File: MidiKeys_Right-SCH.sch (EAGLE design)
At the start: 7 parts

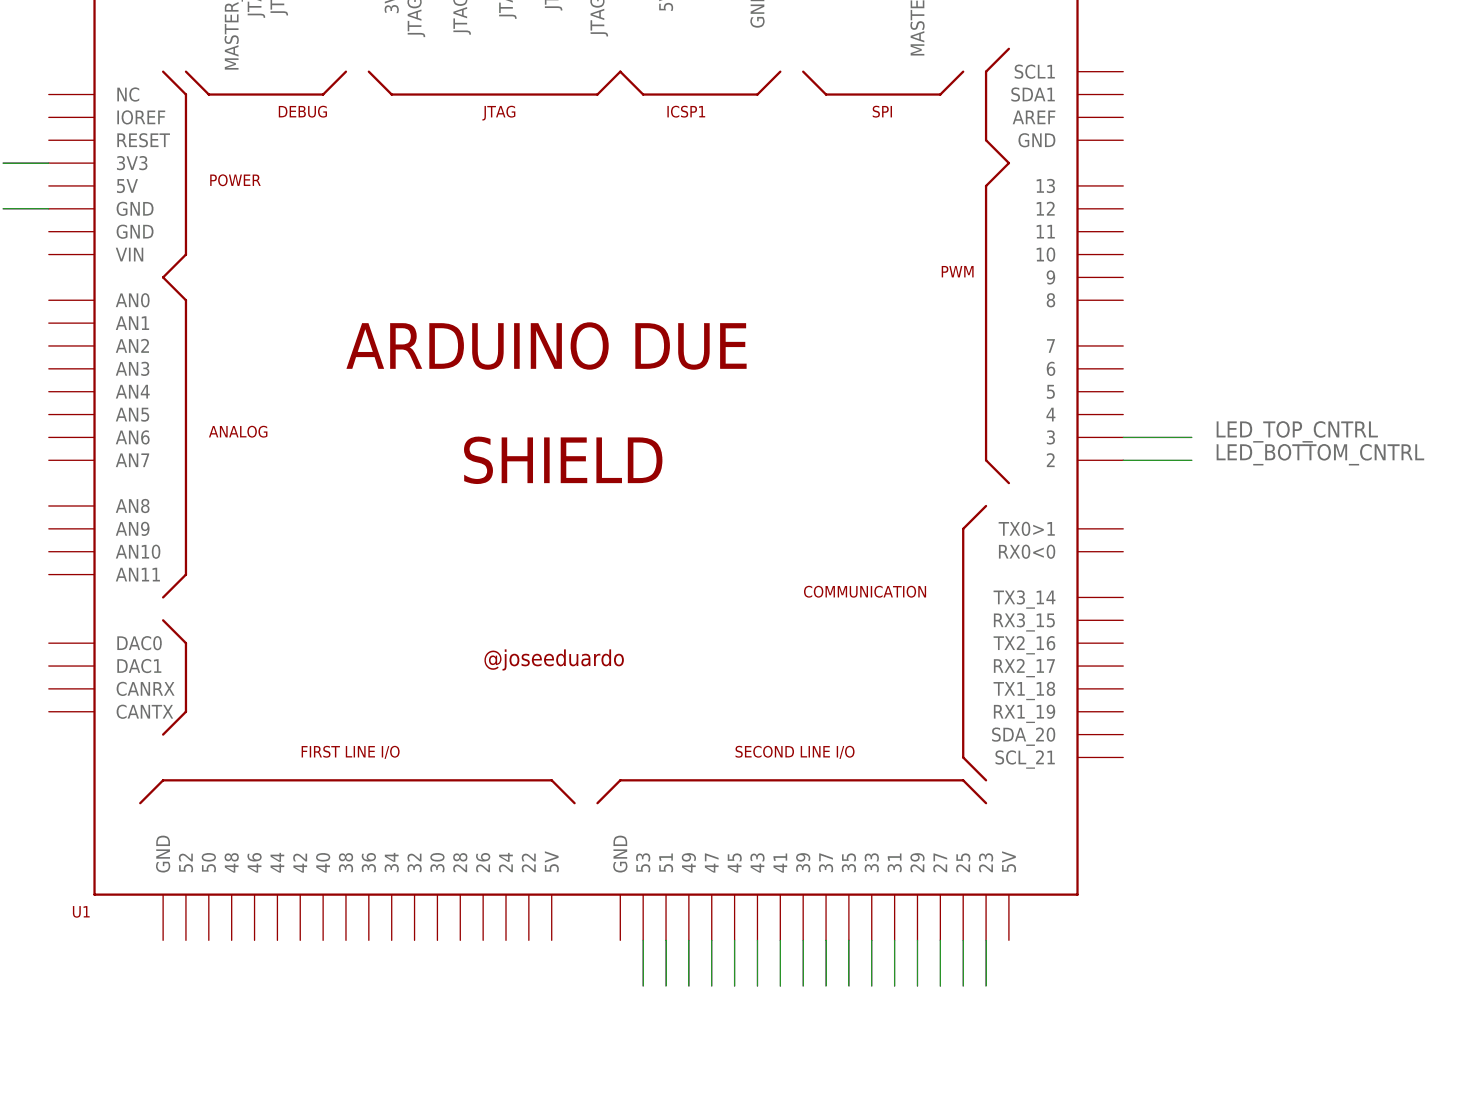
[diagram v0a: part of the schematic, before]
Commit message: added all key nets
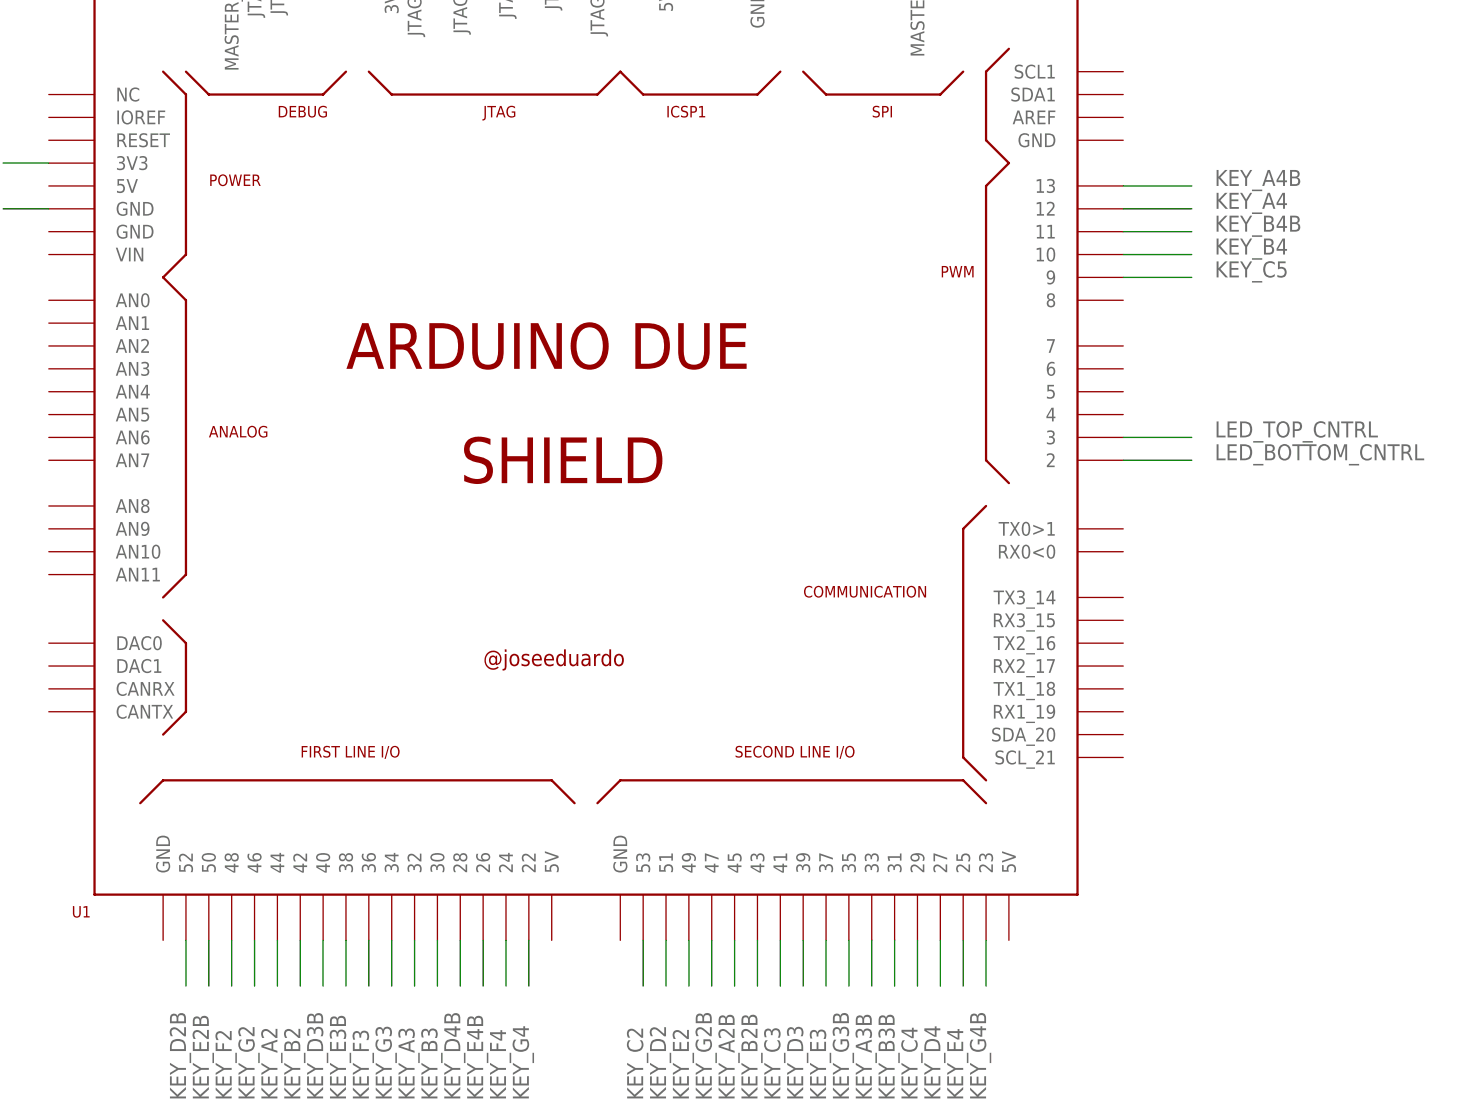
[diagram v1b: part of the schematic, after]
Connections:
- net N$10 renamed KEY_D3
- net N$11 renamed KEY_E3
- net N$12 renamed KEY_G3B
- net N$13 renamed KEY_A3B
- net N$14 renamed KEY_B3B
- net N$15 renamed KEY_C4
- net N$16 renamed KEY_D4
- net N$17 renamed KEY_E4
- net N$18 renamed KEY_G4B
- net N$2 renamed KEY_D2
- net N$3 renamed KEY_E2
- net N$6 renamed KEY_G2B
- net N$7 renamed KEY_A2B
- net N$8 renamed KEY_B2B
- net N$9 renamed KEY_C3
- removed net N$1: ARDUINO_DUE1.53
- new net KEY_A2: ARDUINO_DUE1.44
- new net KEY_A3: ARDUINO_DUE1.32
- new net KEY_A4: ARDUINO_DUE1.12
- new net KEY_A4B: ARDUINO_DUE1.13
- new net KEY_B2: ARDUINO_DUE1.42
- new net KEY_B3: ARDUINO_DUE1.30
- new net KEY_B4: ARDUINO_DUE1.10
- new net KEY_B4B: ARDUINO_DUE1.11
- new net KEY_C5: ARDUINO_DUE1.9
- new net KEY_D3B: ARDUINO_DUE1.40
- new net KEY_D4B: ARDUINO_DUE1.28
- new net KEY_E2B: ARDUINO_DUE1.50
- new net KEY_E3B: ARDUINO_DUE1.38
- new net KEY_E4B: ARDUINO_DUE1.26
- new net KEY_F2: ARDUINO_DUE1.48
- new net KEY_F3: ARDUINO_DUE1.36
- new net KEY_F4: ARDUINO_DUE1.24
- new net KEY_G2: ARDUINO_DUE1.46
- new net KEY_G3: ARDUINO_DUE1.34
- new net KEY_G4: ARDUINO_DUE1.22
- net KEY_C2: now also ARDUINO_DUE1.53
- net KEY_D2B: now also ARDUINO_DUE1.52

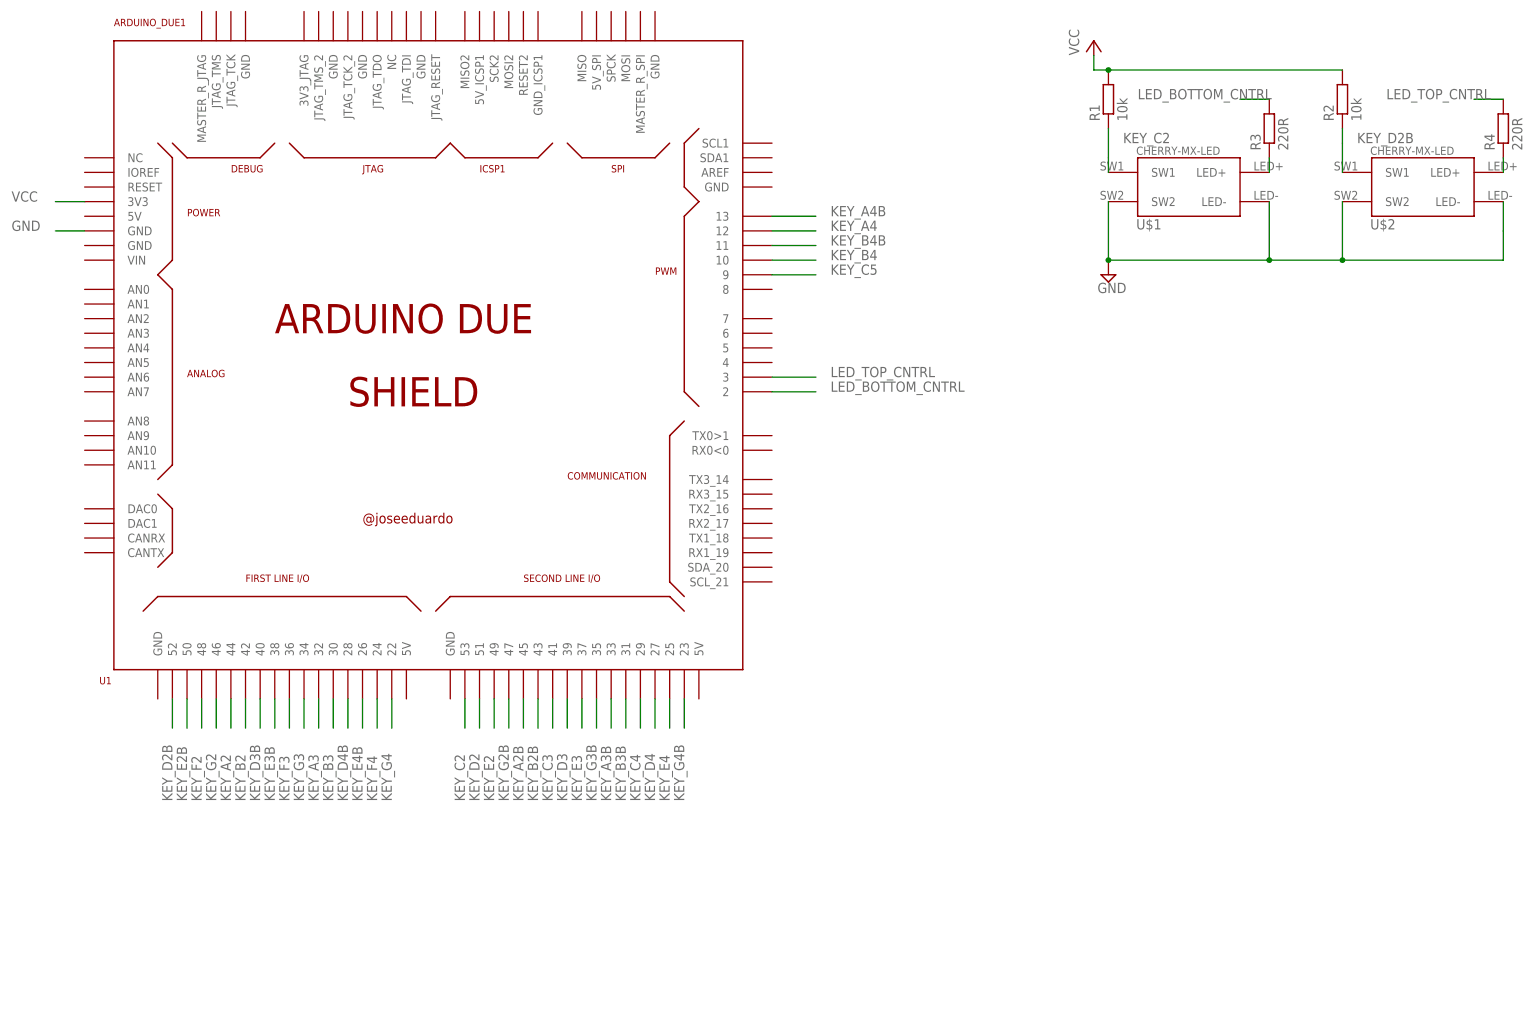
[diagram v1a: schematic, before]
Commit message: cleaned up keys - now adding all of them to schematic
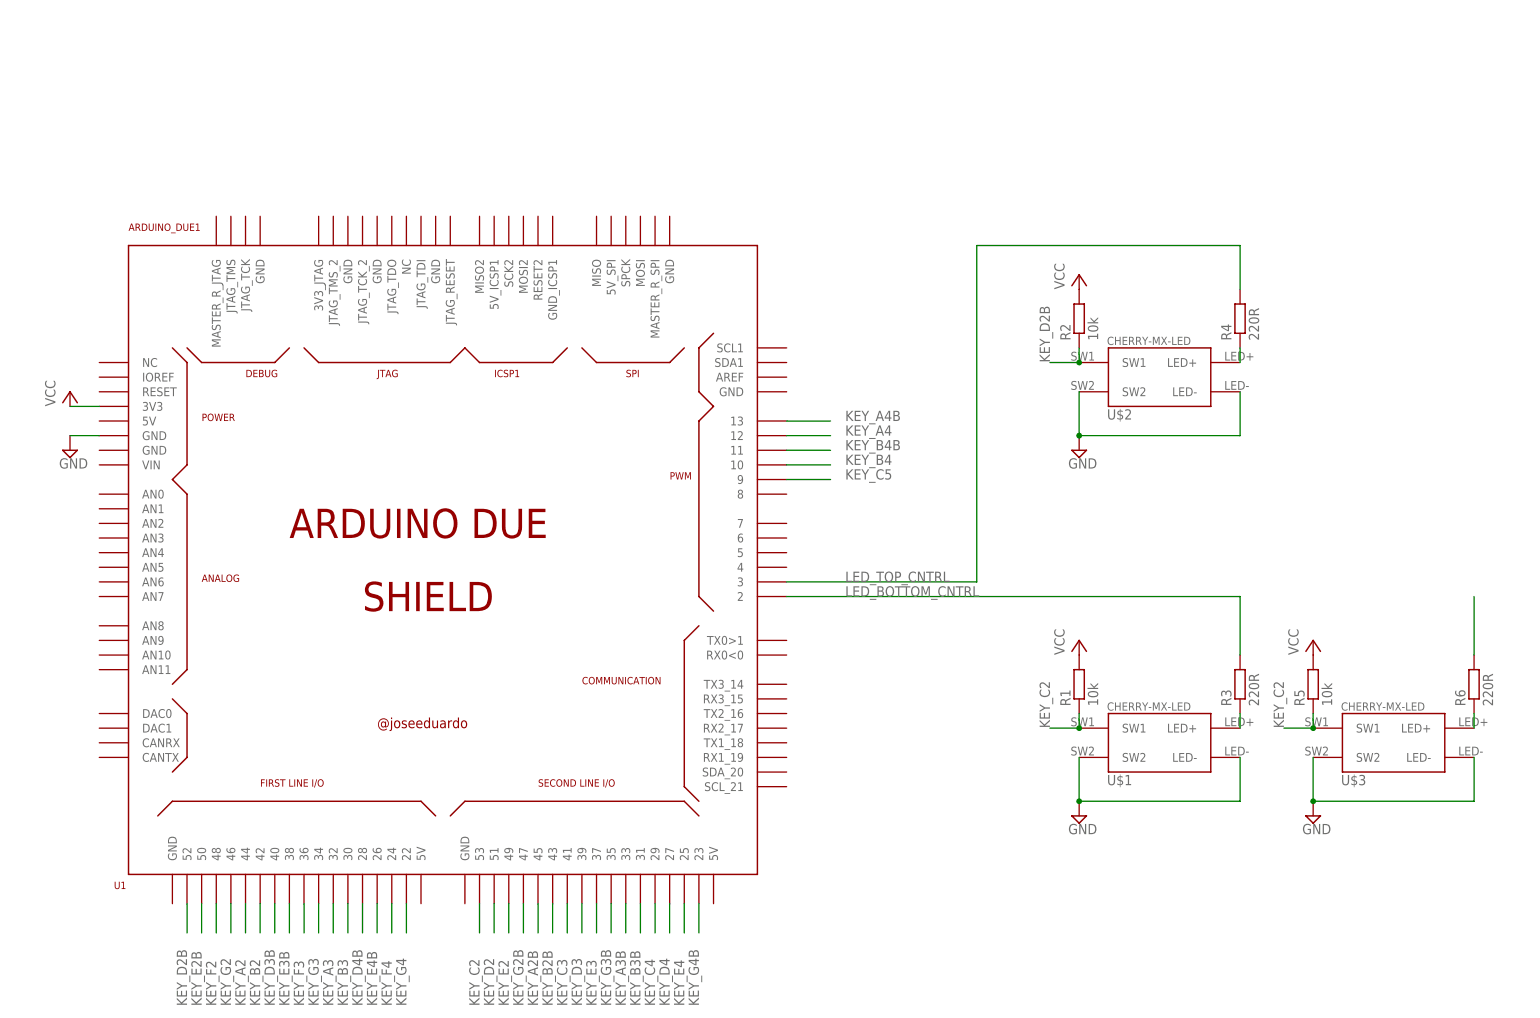
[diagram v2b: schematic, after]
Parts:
- added R5: 10k, resistor:R-EU_R0603
- added R6: 220R, resistor:R-EU_R0603
- added U$3: CHERRY-MX-LED, cherrymx:CHERRY-MX-LED
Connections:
- new net LED_BOTTOM_CNTRL1: R6.2
- new net N$1: R6.1, U$3.LED+
- net GND: now also U$3.LED-, U$3.SW2
- net KEY_C2: now also R5.1, U$3.SW1
- net VCC: now also R5.2
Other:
- moved on the sheet: ARDUINO_DUE1, R1, R2, R3, R4, U$1, U$2

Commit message: created bottom row of keys in schematic
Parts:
- added R10, R12, R14, R16, R18, R20, R22, R24, R26, R28, R30, R32, R34, R36, R38, R40, R42, R44, R46, R48, R8: 220R, resistor:R-EU_R0603
- added R11, R13, R15, R17, R19, R21, R23, R25, R27, R29, R31, R33, R35, R37, R39, R41, R43, R45, R47, R7, R9: 10k, resistor:R-EU_R0603
- added U$10, U$11, U$12, U$13, U$14, U$15, U$16, U$17, U$18, U$19, U$20, U$21, U$22, U$23, U$24, U$4, U$5, U$6, U$7, U$8, U$9: CHERRY-MX-LED, cherrymx:CHERRY-MX-LED
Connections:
- removed net LED_BOTTOM_CNTRL1: R6.2
- new net LED_TOP_CNTRL1: R48.2
- new net N$10: R20.1, U$10.LED+
- new net N$11: R22.1, U$11.LED+
- new net N$12: R24.1, U$12.LED+
- new net N$13: R26.1, U$13.LED+
- new net N$14: R28.1, U$14.LED+
- new net N$15: R30.1, U$15.LED+
- new net N$16: R32.1, U$16.LED+
- new net N$17: R34.1, U$17.LED+
- new net N$18: R36.1, U$18.LED+
- new net N$19: R38.1, U$19.LED+
- new net N$2: R8.1, U$4.LED+
- new net N$20: R40.1, U$20.LED+
- new net N$21: R42.1, U$21.LED+
- new net N$22: R44.1, U$22.LED+
- new net N$23: R46.1, U$23.LED+
- new net N$24: R48.1, U$24.LED+
- new net N$3: R10.1, U$5.LED+
- new net N$6: R12.1, U$6.LED+
- new net N$7: R14.1, U$7.LED+
- new net N$8: R16.1, U$8.LED+
- new net N$9: R18.1, U$9.LED+
- net GND: now also U$10.LED-, U$10.SW2, U$11.LED-, U$11.SW2, U$12.LED-, U$12.SW2, U$13.LED-, U$13.SW2, U$14.LED-, U$14.SW2, U$15.LED-, U$15.SW2, U$16.LED-, U$16.SW2, U$17.LED-, U$17.SW2, U$18.LED-, U$18.SW2, U$19.LED-, U$19.SW2, U$20.LED-, U$20.SW2, U$21.LED-, U$21.SW2, U$22.LED-, U$22.SW2, U$23.LED-, U$23.SW2, U$24.LED-, U$24.SW2, U$4.LED-, U$4.SW2, U$5.LED-, U$5.SW2, U$6.LED-, U$6.SW2, U$7.LED-, U$7.SW2, U$8.LED-, U$8.SW2, U$9.LED-, U$9.SW2
- net KEY_A2: now also R13.1, U$7.SW1
- net KEY_A3: now also R27.1, U$14.SW1
- net KEY_A4: now also R41.1, U$21.SW1
- net KEY_B2: now also R15.1, U$8.SW1
- net KEY_B3: now also R29.1, U$15.SW1
- net KEY_B4: now also R43.1, U$22.SW1
- net KEY_C2: no longer R5.1, U$3.SW1
- net KEY_C3: now also R17.1, U$9.SW1
- net KEY_C4: now also R31.1, U$16.SW1
- net KEY_C5: now also R45.1, U$23.SW1
- net KEY_D2: now also R5.1, U$3.SW1
- net KEY_D3: now also R19.1, U$10.SW1
- net KEY_D4: now also R33.1, U$17.SW1
- net KEY_E2: now also R7.1, U$4.SW1
- net KEY_E3: now also R21.1, U$11.SW1
- net KEY_E4: now also R35.1, U$18.SW1
- net KEY_F2: now also R9.1, U$5.SW1
- net KEY_F3: now also R23.1, U$12.SW1
- net KEY_F4: now also R37.1, U$19.SW1
- net KEY_G2: now also R11.1, U$6.SW1
- net KEY_G3: now also R25.1, U$13.SW1
- net KEY_G4: now also R39.1, U$20.SW1
- net LED_BOTTOM_CNTRL: now also R10.2, R12.2, R14.2, R16.2, R18.2, R20.2, R22.2, R24.2, R26.2, R28.2, R30.2, R32.2, R34.2, R36.2, R38.2, R40.2, R42.2, R44.2, R46.2, R6.2, R8.2
- net VCC: now also R11.2, R13.2, R15.2, R17.2, R19.2, R21.2, R23.2, R25.2, R27.2, R29.2, R31.2, R33.2, R35.2, R37.2, R39.2, R41.2, R43.2, R45.2, R47.2, R7.2, R9.2

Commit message: wired up all keys and assigned net and component names@
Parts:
- added A2B, A3B, A4B, B2B, B3B, B4B, D3B, D4B, E3B, E4B, G2B, G3B, G4B: CHERRY-MX-LED, cherrymx:CHERRY-MX-LED
- added R49, R51, R53, R55, R57, R59, R61, R63, R65, R67, R69, R71, R73: 10k, resistor:R-EU_R0603
- added R50, R52, R54, R56, R58, R60, R62, R64, R66, R68, R70, R72, R74: 220R, resistor:R-EU_R0603
- renumbered U$1 to C2, U$10 to D3, U$11 to E3, U$12 to F3, U$13 to G3, U$14 to A3, U$15 to B3, U$16 to C4, U$17 to D4, U$18 to E4, U$19 to F4, U$2 to D2B, U$20 to G4, U$21 to A4, U$22 to B4, U$23 to C5, U$24 to E2B, U$3 to D2, U$4 to E2, U$5 to F2, U$6 to G2, U$7 to A2, U$8 to B2, U$9 to C3
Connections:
- removed net LED_TOP_CNTRL1: R48.2
- new net N$25: G2B.LED+, R50.1
- new net N$26: A2B.LED+, R52.1
- new net N$27: B2B.LED+, R54.1
- new net N$28: D3B.LED+, R56.1
- new net N$29: E3B.LED+, R58.1
- new net N$30: G3B.LED+, R60.1
- new net N$31: A3B.LED+, R62.1
- new net N$32: B3B.LED+, R64.1
- new net N$33: D4B.LED+, R66.1
- new net N$34: E4B.LED+, R68.1
- new net N$35: G4B.LED+, R70.1
- new net N$36: A4B.LED+, R72.1
- new net N$37: B4B.LED+, R74.1
- net GND: now also A2B.LED-, A2B.SW2, A3B.LED-, A3B.SW2, A4B.LED-, A4B.SW2, B2B.LED-, B2B.SW2, B3B.LED-, B3B.SW2, B4B.LED-, B4B.SW2, D3B.LED-, D3B.SW2, D4B.LED-, D4B.SW2, E3B.LED-, E3B.SW2, E4B.LED-, E4B.SW2, G2B.LED-, G2B.SW2, G3B.LED-, G3B.SW2, G4B.LED-, G4B.SW2
- net KEY_A2B: now also A2B.SW1, R51.1
- net KEY_A3B: now also A3B.SW1, R61.1
- net KEY_A4B: now also A4B.SW1, R71.1
- net KEY_B2B: now also B2B.SW1, R53.1
- net KEY_B3B: now also B3B.SW1, R63.1
- net KEY_B4B: now also B4B.SW1, R73.1
- net KEY_D3B: now also D3B.SW1, R55.1
- net KEY_D4B: now also D4B.SW1, R65.1
- net KEY_E2B: now also E2B.SW1, R47.1
- net KEY_E3B: now also E3B.SW1, R57.1
- net KEY_E4B: now also E4B.SW1, R67.1
- net KEY_G2B: now also G2B.SW1, R49.1
- net KEY_G3B: now also G3B.SW1, R59.1
- net KEY_G4B: now also G4B.SW1, R69.1
- net LED_TOP_CNTRL: now also R48.2, R50.2, R52.2, R54.2, R56.2, R58.2, R60.2, R62.2, R64.2, R66.2, R68.2, R70.2, R72.2, R74.2
- net VCC: now also R49.2, R51.2, R53.2, R55.2, R57.2, R59.2, R61.2, R63.2, R65.2, R67.2, R69.2, R71.2, R73.2

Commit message: added transistor led driver circuit@
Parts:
- added R75, R76: 1K65, resistor:R-EU_R0603
- added T1, T2: 2N2222, adafruit:2N2222
- R10, R12, R14, R16, R18, R20, R22, R24, R26, R28, R3, R30, R32, R34, R36, R38, R4, R40, R42, R44, R46, R48, R50, R52, R54, R56, R58, R6, R60, R62, R64, R66, R68, R70, R72, R74, R8: value 220R -> 82R
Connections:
- removed net LED_BOTTOM_CNTRL: ARDUINO_DUE1.2, R10.2, R12.2, R14.2, R16.2, R18.2, R20.2, R22.2, R24.2, R26.2, R28.2, R3.2, R30.2, R32.2, R34.2, R36.2, R38.2, R40.2, R42.2, R44.2, R46.2, R6.2, R8.2
- removed net LED_TOP_CNTRL: ARDUINO_DUE1.3, R4.2, R48.2, R50.2, R52.2, R54.2, R56.2, R58.2, R60.2, R62.2, R64.2, R66.2, R68.2, R70.2, R72.2, R74.2
- new net LED_CNTRL_BOTTOM: ARDUINO_DUE1.2, R76.1
- new net LED_CNTRL_TOP: ARDUINO_DUE1.3, R75.1
- new net N$65: A2B.LED-, A3B.LED-, A4B.LED-, B2B.LED-, B3B.LED-, B4B.LED-, D2B.LED-, D3B.LED-, D4B.LED-, E2B.LED-, E3B.LED-, E4B.LED-, G2B.LED-, G3B.LED-, G4B.LED-, T2.C
- new net N$74: A2.LED-, A3.LED-, A4.LED-, B2.LED-, B3.LED-, B4.LED-, C2.LED-, C3.LED-, C4.LED-, C5.LED-, D2.LED-, D3.LED-, D4.LED-, E2.LED-, E3.LED-, E4.LED-, F2.LED-, F3.LED-, F4.LED-, G2.LED-, G3.LED-, G4.LED-, T1.C
- new net N$75: R75.2, T2.B
- new net N$76: R76.2, T1.B
- net GND: now also T1.E, T2.E; no longer A2.LED-, A2B.LED-, A3.LED-, A3B.LED-, A4.LED-, A4B.LED-, B2.LED-, B2B.LED-, B3.LED-, B3B.LED-, B4.LED-, B4B.LED-, C2.LED-, C3.LED-, C4.LED-, C5.LED-, D2.LED-, D2B.LED-, D3.LED-, D3B.LED-, D4.LED-, D4B.LED-, E2.LED-, E2B.LED-, E3.LED-, E3B.LED-, E4.LED-, E4B.LED-, F2.LED-, F3.LED-, F4.LED-, G2.LED-, G2B.LED-, G3.LED-, G3B.LED-, G4.LED-, G4B.LED-
- net VCC: now also R10.2, R12.2, R14.2, R16.2, R18.2, R20.2, R22.2, R24.2, R26.2, R28.2, R3.2, R30.2, R32.2, R34.2, R36.2, R38.2, R4.2, R40.2, R42.2, R44.2, R46.2, R48.2, R50.2, R52.2, R54.2, R56.2, R58.2, R6.2, R60.2, R62.2, R64.2, R66.2, R68.2, R70.2, R72.2, R74.2, R8.2
